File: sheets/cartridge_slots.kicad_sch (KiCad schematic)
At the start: 3 parts, among them CN4 AXC90020, CN5 AXC90020, U33 74HC04

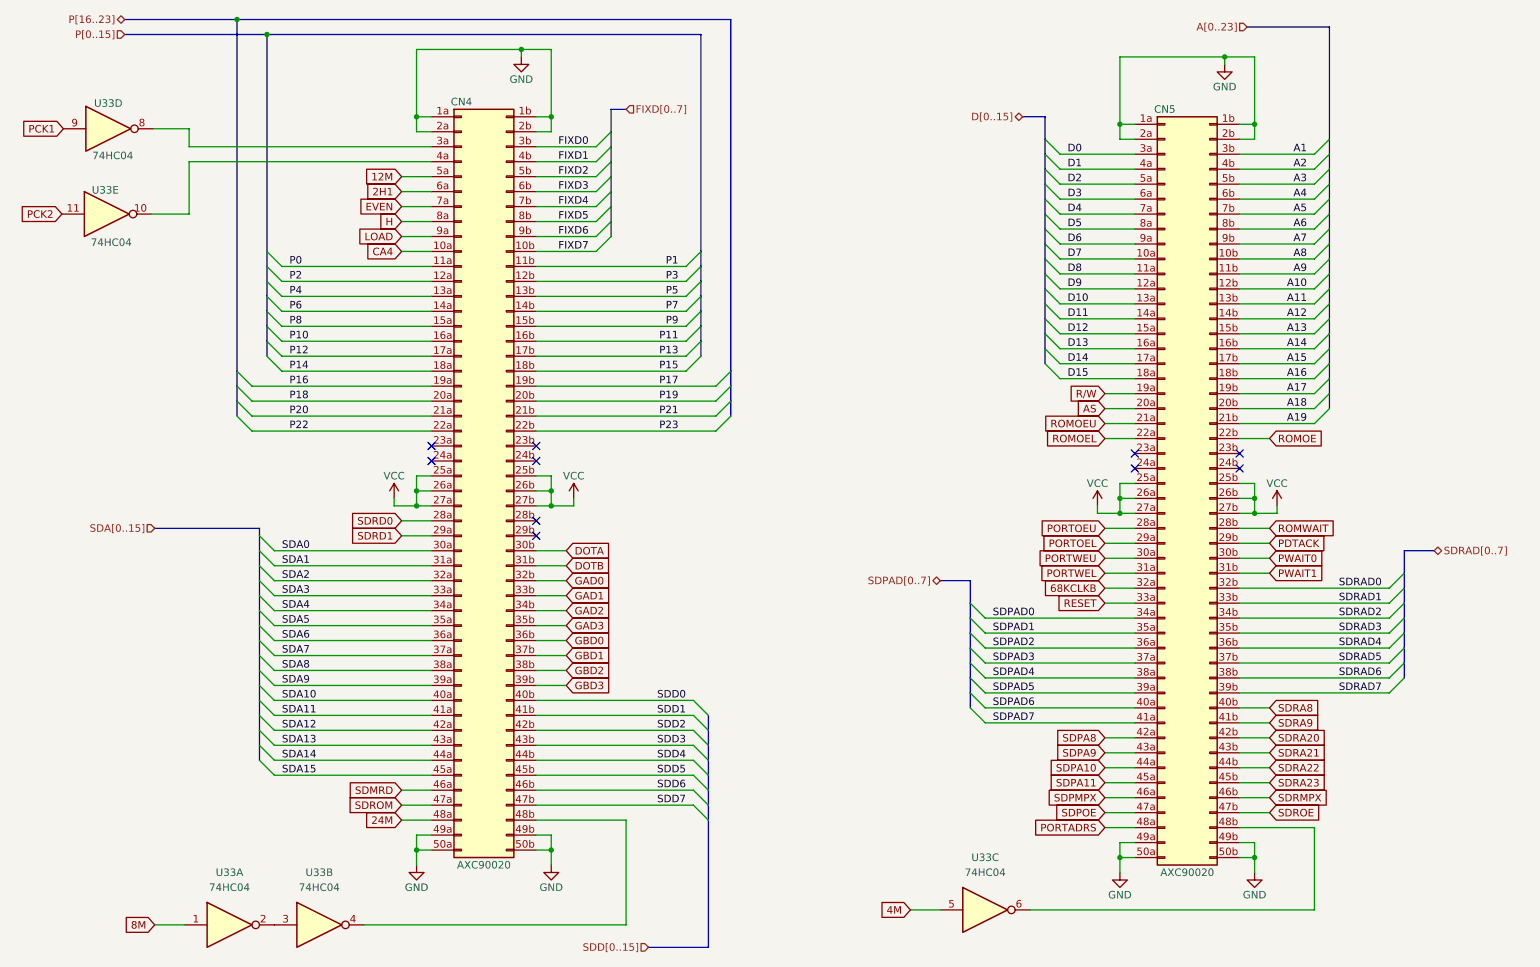
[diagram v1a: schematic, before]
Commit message: Updated Footprints
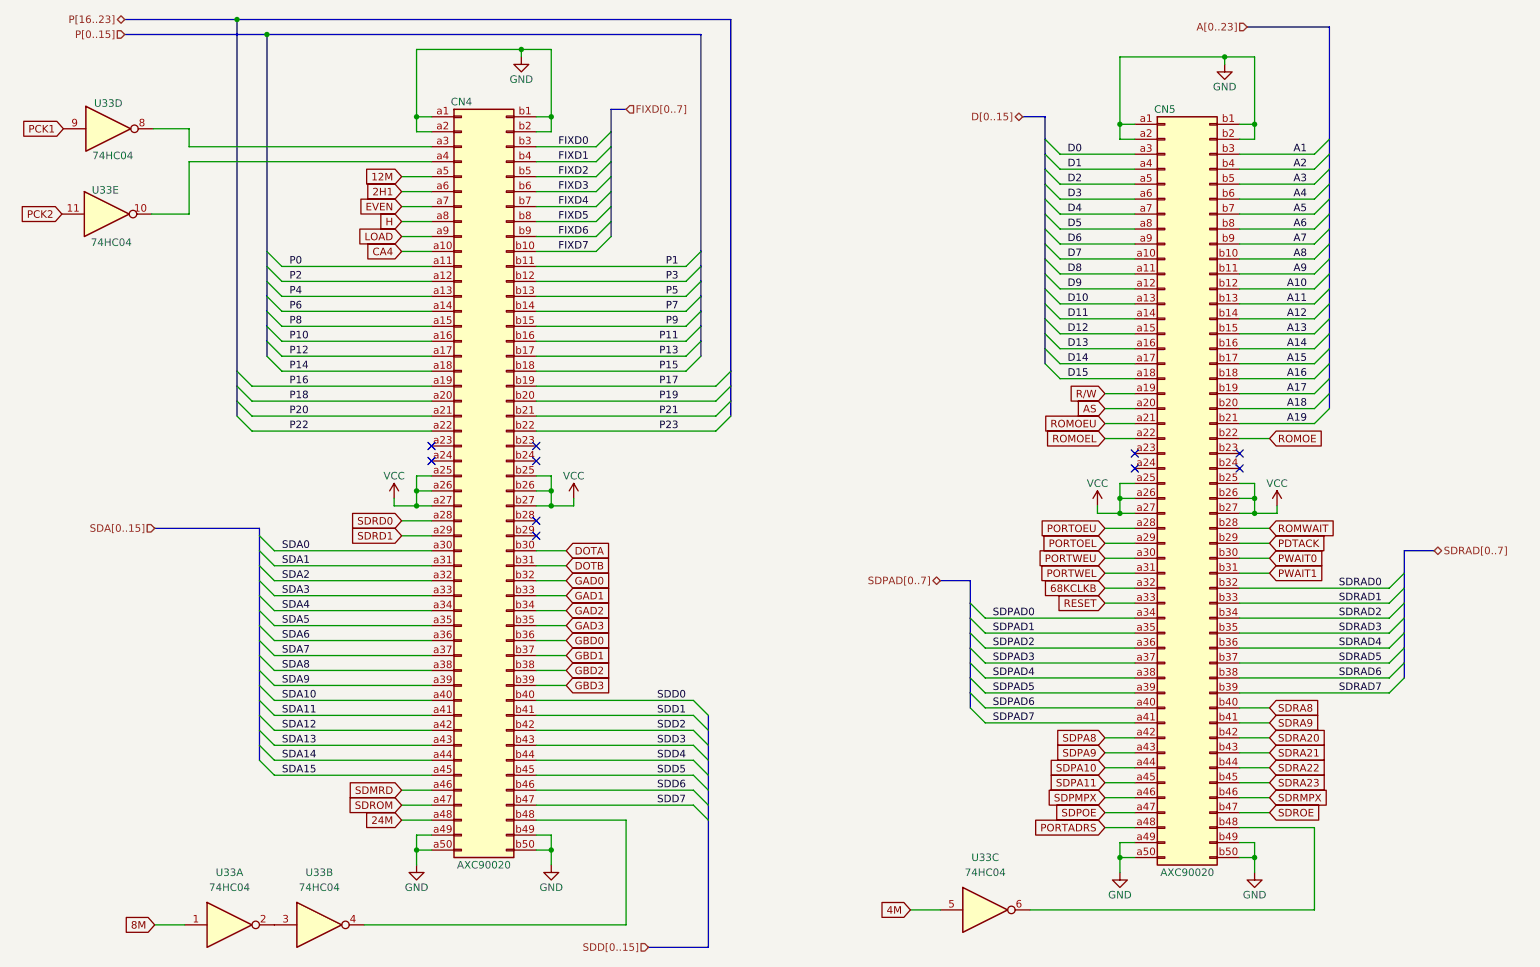
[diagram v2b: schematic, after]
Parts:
- CN4, CN5: footprint (none) -> 1_NeoGeoLibrary:AXC90020
- U33: footprint (none) -> Package_DIP:DIP-14_W7.62mm
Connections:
- net 12M: now also CN4.a5; no longer CN4.5a (Pin_5a)
- net 24M: now also CN4.a48; no longer CN4.48a (Pin_48a)
- net 2H1: now also CN4.a6; no longer CN4.6a (Pin_6a)
- net 68KCLKB: now also CN5.a32; no longer CN5.32a (Pin_32a)
- net A1: now also CN5.b3; no longer CN5.3b (Pin_3b)
- net A10: now also CN5.b12; no longer CN5.12b (Pin_12b)
- net A11: now also CN5.b13; no longer CN5.13b (Pin_13b)
- net A12: now also CN5.b14; no longer CN5.14b (Pin_14b)
- net A13: now also CN5.b15; no longer CN5.15b (Pin_15b)
- net A14: now also CN5.b16; no longer CN5.16b (Pin_16b)
- net A15: now also CN5.b17; no longer CN5.17b (Pin_17b)
- net A16: now also CN5.b18; no longer CN5.18b (Pin_18b)
- net A17: now also CN5.b19; no longer CN5.19b (Pin_19b)
- net A18: now also CN5.b20; no longer CN5.20b (Pin_20b)
- net A19: now also CN5.b21; no longer CN5.21b (Pin_21b)
- net A2: now also CN5.b4; no longer CN5.4b (Pin_4b)
- net A3: now also CN5.b5; no longer CN5.5b (Pin_5b)
- net A4: now also CN5.b6; no longer CN5.6b (Pin_6b)
- net A5: now also CN5.b7; no longer CN5.7b (Pin_7b)
- net A6: now also CN5.b8; no longer CN5.8b (Pin_8b)
- net A7: now also CN5.b9; no longer CN5.9b (Pin_9b)
- net A8: now also CN5.b10; no longer CN5.10b (Pin_10b)
- net A9: now also CN5.b11; no longer CN5.11b (Pin_11b)
- net AS: now also CN5.a20; no longer CN5.20a (Pin_20a)
- net CA4: now also CN4.a10; no longer CN4.10a (Pin_10a)
- net D0: now also CN5.a3; no longer CN5.3a (Pin_3a)
- net D1: now also CN5.a4; no longer CN5.4a (Pin_4a)
- net D10: now also CN5.a13; no longer CN5.13a (Pin_13a)
- net D11: now also CN5.a14; no longer CN5.14a (Pin_14a)
- net D12: now also CN5.a15; no longer CN5.15a (Pin_15a)
- net D13: now also CN5.a16; no longer CN5.16a (Pin_16a)
- net D14: now also CN5.a17; no longer CN5.17a (Pin_17a)
- net D15: now also CN5.a18; no longer CN5.18a (Pin_18a)
- net D2: now also CN5.a5; no longer CN5.5a (Pin_5a)
- net D3: now also CN5.a6; no longer CN5.6a (Pin_6a)
- net D4: now also CN5.a7; no longer CN5.7a (Pin_7a)
- net D5: now also CN5.a8; no longer CN5.8a (Pin_8a)
- net D6: now also CN5.a9; no longer CN5.9a (Pin_9a)
- net D7: now also CN5.a10; no longer CN5.10a (Pin_10a)
- net D8: now also CN5.a11; no longer CN5.11a (Pin_11a)
- net D9: now also CN5.a12; no longer CN5.12a (Pin_12a)
- net DOTA: now also CN4.b30; no longer CN4.30b (Pin_30b)
- net DOTB: now also CN4.b31; no longer CN4.31b (Pin_31b)
- net EVEN: now also CN4.a7; no longer CN4.7a (Pin_7a)
- net FIXD0: now also CN4.b3; no longer CN4.3b (Pin_3b)
- net FIXD1: now also CN4.b4; no longer CN4.4b (Pin_4b)
- net FIXD2: now also CN4.b5; no longer CN4.5b (Pin_5b)
- net FIXD3: now also CN4.b6; no longer CN4.6b (Pin_6b)
- net FIXD4: now also CN4.b7; no longer CN4.7b (Pin_7b)
- net FIXD5: now also CN4.b8; no longer CN4.8b (Pin_8b)
- net FIXD6: now also CN4.b9; no longer CN4.9b (Pin_9b)
- net FIXD7: now also CN4.b10; no longer CN4.10b (Pin_10b)
- net GAD0: now also CN4.b32; no longer CN4.32b (Pin_32b)
- net GAD1: now also CN4.b33; no longer CN4.33b (Pin_33b)
- net GAD2: now also CN4.b34; no longer CN4.34b (Pin_34b)
- net GAD3: now also CN4.b35; no longer CN4.35b (Pin_35b)
- net GBD0: now also CN4.b36; no longer CN4.36b (Pin_36b)
- net GBD1: now also CN4.b37; no longer CN4.37b (Pin_37b)
- net GBD2: now also CN4.b38; no longer CN4.38b (Pin_38b)
- net GBD3: now also CN4.b39; no longer CN4.39b (Pin_39b)
- net GND: now also CN4.a1, CN4.a2, CN4.a49, CN4.a50, CN4.b1, CN4.b2, CN4.b49, CN4.b50, CN5.a1, CN5.a2, CN5.a49, CN5.a50, CN5.b1, CN5.b2, CN5.b49, CN5.b50; no longer CN4.1a (Pin_1a), CN4.1b (Pin_1b), CN4.2a (Pin_2a), CN4.2b (Pin_2b), CN4.49a (Pin_49a), CN4.49b (Pin_49b), CN4.50a (Pin_50a), CN4.50b (Pin_50b), CN5.1a (Pin_1a), CN5.1b (Pin_1b), CN5.2a (Pin_2a), CN5.2b (Pin_2b), CN5.49a (Pin_49a), CN5.49b (Pin_49b), CN5.50a (Pin_50a), CN5.50b (Pin_50b)
- net H: now also CN4.a8; no longer CN4.8a (Pin_8a)
- net LOAD: now also CN4.a9; no longer CN4.9a (Pin_9a)
- net P0: now also CN4.a11; no longer CN4.11a (Pin_11a)
- net P1: now also CN4.b11; no longer CN4.11b (Pin_11b)
- net P10: now also CN4.a16; no longer CN4.16a (Pin_16a)
- net P11: now also CN4.b16; no longer CN4.16b (Pin_16b)
- net P12: now also CN4.a17; no longer CN4.17a (Pin_17a)
- net P13: now also CN4.b17; no longer CN4.17b (Pin_17b)
- net P14: now also CN4.a18; no longer CN4.18a (Pin_18a)
- net P15: now also CN4.b18; no longer CN4.18b (Pin_18b)
- net P16: now also CN4.a19; no longer CN4.19a (Pin_19a)
- net P17: now also CN4.b19; no longer CN4.19b (Pin_19b)
- net P18: now also CN4.a20; no longer CN4.20a (Pin_20a)
- net P19: now also CN4.b20; no longer CN4.20b (Pin_20b)
- net P2: now also CN4.a12; no longer CN4.12a (Pin_12a)
- net P20: now also CN4.a21; no longer CN4.21a (Pin_21a)
- net P21: now also CN4.b21; no longer CN4.21b (Pin_21b)
- net P22: now also CN4.a22; no longer CN4.22a (Pin_22a)
- net P23: now also CN4.b22; no longer CN4.22b (Pin_22b)
- net P3: now also CN4.b12; no longer CN4.12b (Pin_12b)
- net P4: now also CN4.a13; no longer CN4.13a (Pin_13a)
- net P5: now also CN4.b13; no longer CN4.13b (Pin_13b)
- net P6: now also CN4.a14; no longer CN4.14a (Pin_14a)
- net P7: now also CN4.b14; no longer CN4.14b (Pin_14b)
- net P8: now also CN4.a15; no longer CN4.15a (Pin_15a)
- net P9: now also CN4.b15; no longer CN4.15b (Pin_15b)
- net PDTACK: now also CN5.b29; no longer CN5.29b (Pin_29b)
- net PORTADRS: now also CN5.a48; no longer CN5.48a (Pin_48a)
- net PORTOEL: now also CN5.a29; no longer CN5.29a (Pin_29a)
- net PORTOEU: now also CN5.a28; no longer CN5.28a (Pin_28a)
- net PORTWEL: now also CN5.a31; no longer CN5.31a (Pin_31a)
- net PORTWEU: now also CN5.a30; no longer CN5.30a (Pin_30a)
- net PWAIT0: now also CN5.b30; no longer CN5.30b (Pin_30b)
- net PWAIT1: now also CN5.b31; no longer CN5.31b (Pin_31b)
- net RESET: now also CN5.a33; no longer CN5.33a (Pin_33a)
- net ROMOE: now also CN5.b22; no longer CN5.22b (Pin_22b)
- net ROMOEL: now also CN5.a22; no longer CN5.22a (Pin_22a)
- net ROMOEU: now also CN5.a21; no longer CN5.21a (Pin_21a)
- net ROMWAIT: now also CN5.b28; no longer CN5.28b (Pin_28b)
- net R/W: now also CN5.a19; no longer CN5.19a (Pin_19a)
- net SDA0: now also CN4.a30; no longer CN4.30a (Pin_30a)
- net SDA1: now also CN4.a31; no longer CN4.31a (Pin_31a)
- net SDA10: now also CN4.a40; no longer CN4.40a (Pin_40a)
- net SDA11: now also CN4.a41; no longer CN4.41a (Pin_41a)
- net SDA12: now also CN4.a42; no longer CN4.42a (Pin_42a)
- net SDA13: now also CN4.a43; no longer CN4.43a (Pin_43a)
- net SDA14: now also CN4.a44; no longer CN4.44a (Pin_44a)
- net SDA15: now also CN4.a45; no longer CN4.45a (Pin_45a)
- net SDA2: now also CN4.a32; no longer CN4.32a (Pin_32a)
- net SDA3: now also CN4.a33; no longer CN4.33a (Pin_33a)
- net SDA4: now also CN4.a34; no longer CN4.34a (Pin_34a)
- net SDA5: now also CN4.a35; no longer CN4.35a (Pin_35a)
- net SDA6: now also CN4.a36; no longer CN4.36a (Pin_36a)
- net SDA7: now also CN4.a37; no longer CN4.37a (Pin_37a)
- net SDA8: now also CN4.a38; no longer CN4.38a (Pin_38a)
- net SDA9: now also CN4.a39; no longer CN4.39a (Pin_39a)
- net SDD0: now also CN4.b40; no longer CN4.40b (Pin_40b)
- net SDD1: now also CN4.b41; no longer CN4.41b (Pin_41b)
- net SDD2: now also CN4.b42; no longer CN4.42b (Pin_42b)
- net SDD3: now also CN4.b43; no longer CN4.43b (Pin_43b)
- net SDD4: now also CN4.b44; no longer CN4.44b (Pin_44b)
- net SDD5: now also CN4.b45; no longer CN4.45b (Pin_45b)
- net SDD6: now also CN4.b46; no longer CN4.46b (Pin_46b)
- net SDD7: now also CN4.b47; no longer CN4.47b (Pin_47b)
- net SDMRD: now also CN4.a46; no longer CN4.46a (Pin_46a)
- net SDPA10: now also CN5.a44; no longer CN5.44a (Pin_44a)
- net SDPA11: now also CN5.a45; no longer CN5.45a (Pin_45a)
- net SDPA8: now also CN5.a42; no longer CN5.42a (Pin_42a)
- net SDPA9: now also CN5.a43; no longer CN5.43a (Pin_43a)
- net SDPAD0: now also CN5.a34; no longer CN5.34a (Pin_34a)
- net SDPAD1: now also CN5.a35; no longer CN5.35a (Pin_35a)
- net SDPAD2: now also CN5.a36; no longer CN5.36a (Pin_36a)
- net SDPAD3: now also CN5.a37; no longer CN5.37a (Pin_37a)
- net SDPAD4: now also CN5.a38; no longer CN5.38a (Pin_38a)
- net SDPAD5: now also CN5.a39; no longer CN5.39a (Pin_39a)
- net SDPAD6: now also CN5.a40; no longer CN5.40a (Pin_40a)
- net SDPAD7: now also CN5.a41; no longer CN5.41a (Pin_41a)
- net SDPMPX: now also CN5.a46; no longer CN5.46a (Pin_46a)
- net SDPOE: now also CN5.a47; no longer CN5.47a (Pin_47a)
- net SDRA20: now also CN5.b42; no longer CN5.42b (Pin_42b)
- net SDRA21: now also CN5.b43; no longer CN5.43b (Pin_43b)
- net SDRA22: now also CN5.b44; no longer CN5.44b (Pin_44b)
- net SDRA23: now also CN5.b45; no longer CN5.45b (Pin_45b)
- net SDRA8: now also CN5.b40; no longer CN5.40b (Pin_40b)
- net SDRA9: now also CN5.b41; no longer CN5.41b (Pin_41b)
- net SDRAD0: now also CN5.b32; no longer CN5.32b (Pin_32b)
- net SDRAD1: now also CN5.b33; no longer CN5.33b (Pin_33b)
- net SDRAD2: now also CN5.b34; no longer CN5.34b (Pin_34b)
- net SDRAD3: now also CN5.b35; no longer CN5.35b (Pin_35b)
- net SDRAD4: now also CN5.b36; no longer CN5.36b (Pin_36b)
- net SDRAD5: now also CN5.b37; no longer CN5.37b (Pin_37b)
- net SDRAD6: now also CN5.b38; no longer CN5.38b (Pin_38b)
- net SDRAD7: now also CN5.b39; no longer CN5.39b (Pin_39b)
- net SDRD0: now also CN4.a28; no longer CN4.28a (Pin_28a)
- net SDRD1: now also CN4.a29; no longer CN4.29a (Pin_29a)
- net SDRMPX: now also CN5.b46; no longer CN5.46b (Pin_46b)
- net SDROE: now also CN5.b47; no longer CN5.47b (Pin_47b)
- net SDROM: now also CN4.a47; no longer CN4.47a (Pin_47a)
- net VCC: now also CN4.a25, CN4.a26, CN4.a27, CN4.b25, CN4.b26, CN4.b27, CN5.a25, CN5.a26, CN5.a27, CN5.b25, CN5.b26, CN5.b27; no longer CN4.25a (Pin_25a), CN4.25b (Pin_25b), CN4.26a (Pin_26a), CN4.26b (Pin_26b), CN4.27a (Pin_27a), CN4.27b (Pin_27b), CN5.25a (Pin_25a), CN5.25b (Pin_25b), CN5.26a (Pin_26a), CN5.26b (Pin_26b), CN5.27a (Pin_27a), CN5.27b (Pin_27b)
- net at U33.4: now also CN4.b48; no longer CN4.48b (Pin_48b)
- net at U33.6: now also CN5.b48; no longer CN5.48b (Pin_48b)
- net at U33.10: now also CN4.a4; no longer CN4.4a (Pin_4a)
- net at U33.8: now also CN4.a3; no longer CN4.3a (Pin_3a)
